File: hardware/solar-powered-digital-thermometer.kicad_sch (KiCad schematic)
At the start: 5 parts, among them U1 STM32L010K8Tx, U2 74AHC595, U3 74AHC595, U4 74AHC595, U5 BQ25504

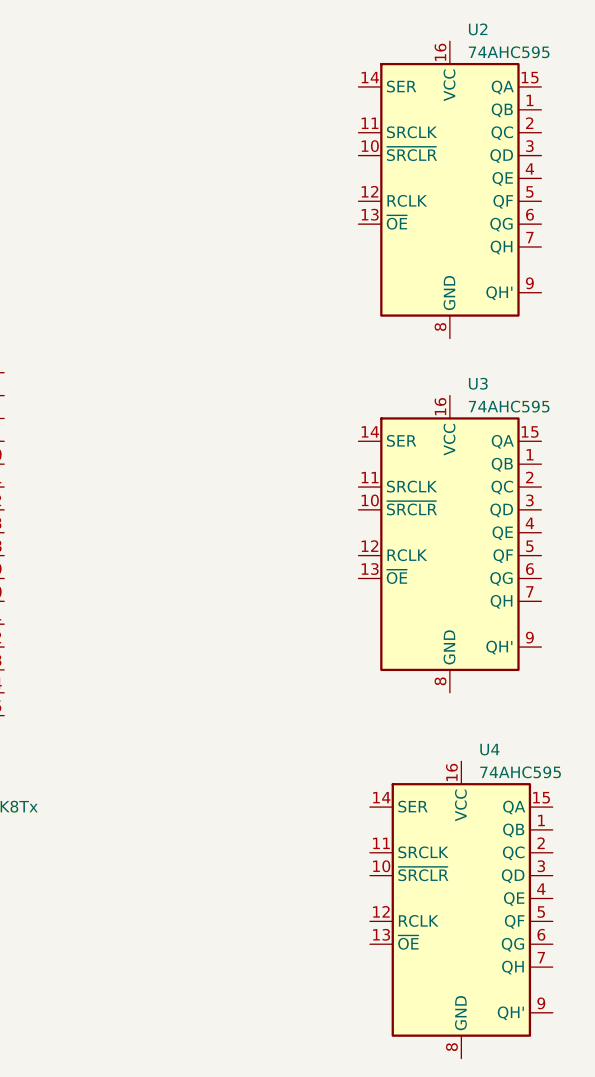
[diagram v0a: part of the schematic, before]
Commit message: add lcd and remove shift registers
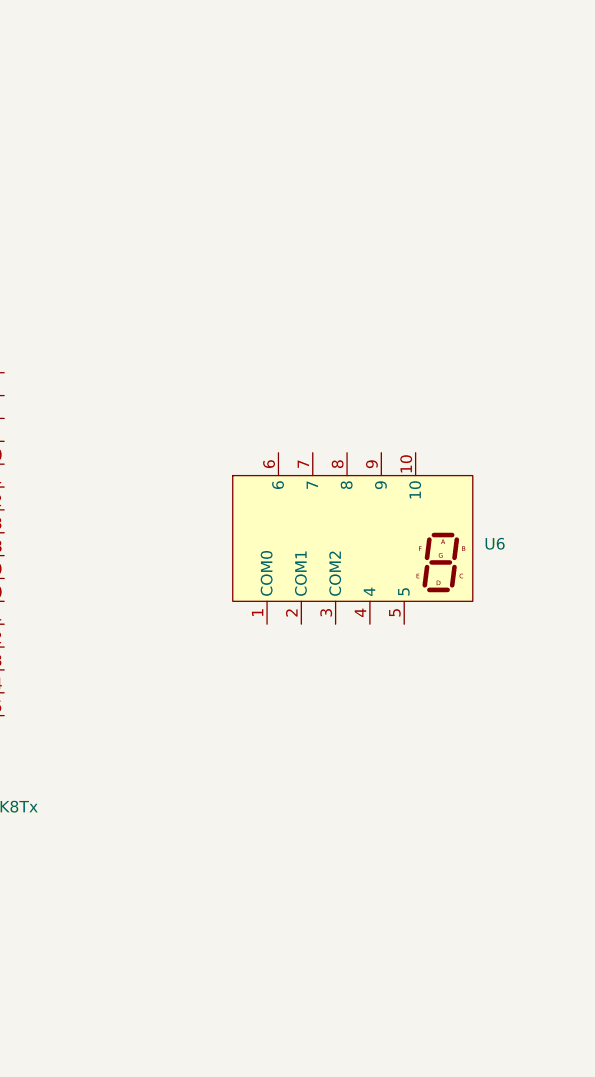
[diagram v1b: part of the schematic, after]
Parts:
- removed U2, U3, U4: 74AHC595, symbol 74xx:74AHC595
- added U6: ~, symbol custom:OD-301
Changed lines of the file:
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@@
     )
   )
-  (symbol (lib_id "74xx:74AHC595") (at 208.28 52.07 0) (unit 1)
+  (symbol (lib_id "custom:OD-301") (at 198.12 92.71 0) (unit 1)
     (in_bom yes) (on_board yes) (dnp no) (fields_autoplaced)
-    (property "Reference" "U2" (at 210.2359 35.56 0)
+    (property "Reference" "U6" (at 212.09 92.71 0)
       (effects (font (size 1.27 1.27)) (justify left))
     )
-    (property "Value" "74AHC595" (at 210.2359 38.1 0)
-      (effects (font (size 1.27 1.27)) (justify left))
+    (property "Value" "~" (at 198.12 92.71 0)
+      (effects (font (size 1.27 1.27)))
     )
-    (property "Footprint" "" (at 208.28 52.07 0)
+    (property "Footprint" "" (at 198.12 92.71 0)
       (effects (font (size 1.27 1.27)) hide)
     )
-    (property "Datasheet" "https://assets.nexperia.com/documents/data-sheet/74AHC_AHCT595.pdf" (at 208.28 52.07 0)
+    (property "Datasheet" "" (at 198.12 92.71 0)
       (effects (font (size 1.27 1.27)) hide)
     )
     (pin "1")
     (pin "10")
-    (pin "11")
-    (pin "12")
-    (pin "13")
-    (pin "14")
-    (pin "15")
-    (pin "16")
     (pin "2")
     (pin "3")
@@
       (project "solar-powered-digital-thermometer"
         (path "/16acc000-7506-41f2-bccc-9839e491fadf"
-          (reference "U2") (unit 1)
-        )
-      )
-    )
-  )
-  (symbol (lib_id "74xx:74AHC595") (at 209.55 132.08 0) (unit 1)
-    (in_bom yes) (on_board yes) (dnp no) (fields_autoplaced)
-    (property "Reference" "U4" (at 211.5059 115.57 0)
-      (effects (font (size 1.27 1.27)) (justify left))
-    )
-    (property "Value" "74AHC595" (at 211.5059 118.11 0)
-      (effects (font (size 1.27 1.27)) (justify left))
-    )
-    (property "Footprint" "" (at 209.55 132.08 0)
-      (effects (font (size 1.27 1.27)) hide)
-    )
-    (property "Datasheet" "https://assets.nexperia.com/documents/data-sheet/74AHC_AHCT595.pdf" (at 209.55 132.08 0)
-      (effects (font (size 1.27 1.27)) hide)
-    )
-    (pin "1")
-    (pin "10")
-    (pin "11")
-    (pin "12")
-    (pin "13")
-    (pin "14")
-    (pin "15")
-    (pin "16")
-    (pin "2")
-    (pin "3")
-    (pin "4")
-    (pin "5")
-    (pin "6")
-    (pin "7")
-    (pin "8")
-    (pin "9")
-    (instances
-      (project "solar-powered-digital-thermometer"
-        (path "/16acc000-7506-41f2-bccc-9839e491fadf"
-          (reference "U4") (unit 1)
+          (reference "U6") (unit 1)
         )
       )
@@
         )
       )
-    )
-  )
-  (symbol (lib_id "74xx:74AHC595") (at 208.28 91.44 0) (unit 1)
-    (in_bom yes) (on_board yes) (dnp no) (fields_autoplaced)
-    (property "Reference" "U3" (at 210.2359 74.93 0)
-      (effects (font (size 1.27 1.27)) (justify left))
-    )
-    (property "Value" "74AHC595" (at 210.2359 77.47 0)
-      (effects (font (size 1.27 1.27)) (justify left))
-    )
-    (property "Footprint" "" (at 208.28 91.44 0)
-      (effects (font (size 1.27 1.27)) hide)
-    )
-    (property "Datasheet" "https://assets.nexperia.com/documents/data-sheet/74AHC_AHCT595.pdf" (at 208.28 91.44 0)
-      (effects (font (size 1.27 1.27)) hide)
-    )
-    (pin "1")
-    (pin "10")
-    (pin "11")
-    (pin "12")
-    (pin "13")
-    (pin "14")
-    (pin "15")
-    (pin "16")
-    (pin "2")
-    (pin "3")
-    (pin "4")
-    (pin "5")
-    (pin "6")
-    (pin "7")
-    (pin "8")
-    (pin "9")
-    (instances
-      (project "solar-powered-digital-thermometer"
-        (path "/16acc000-7506-41f2-bccc-9839e491fadf"
-          (reference "U3") (unit 1)
-        )
-      )

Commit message: add lcd footprint
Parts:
- U6: footprint (none) -> custom:OD-301
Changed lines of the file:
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@@
       (effects (font (size 1.27 1.27)))
     )
-    (property "Footprint" "" (at 198.12 92.71 0)
+    (property "Footprint" "custom:OD-301" (at 198.12 92.71 0)
       (effects (font (size 1.27 1.27)) hide)
     )
